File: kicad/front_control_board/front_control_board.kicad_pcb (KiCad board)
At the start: 2 copper layers, 189.2 x 48.9 mm, 67 parts, among them J1 MAIN_BOARD, J2 PROG, J3 DISPLAY, J4 LED_OUT, Q1 AO3400A, SW1 PEC11R-4215K-S00xx, SW2 BTN1, SW3 BTN4, SW4 BTN2, SW5 BTN3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

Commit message: cleanup
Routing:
- net /TXD0: track 79.4 -> 78.5 mm
- net /DOUT: track 54.2 -> 54.7 mm
- net GND: vias 47 -> 49
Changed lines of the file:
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@@
 	(title_block
 		(title "SW32 - Front Control Board")
-		(date "2024-06-02")
+		(date "2024-06-05")
 		(rev "1")
 		(company "saawsm")
@@
 	)
 	(via
-		(at 163.449 108.331)
+		(at 162.687 107.5436)
 		(size 0.6)
 		(drill 0.3)
@@
 	)
 	(via
+		(at 160.7566 109.0676)
+		(size 0.6)
+		(drill 0.3)
+		(layers "F.Cu" "B.Cu")
+		(locked yes)
+		(free yes)
+		(net 3)
+	)
+	(via
 		(at 180.34 125.603)
 		(size 0.8)
@@
 	)
 	(via
-		(at 165.735 110.617)
+		(at 165.5064 110.4392)
 		(size 0.6)
 		(drill 0.3)
@@
 	)
 	(via
+		(at 164.1856 109.0676)
+		(size 0.6)
+		(drill 0.3)
+		(layers "F.Cu" "B.Cu")
+		(locked yes)
+		(free yes)
+		(net 3)
+	)
+	(via
 		(at 177.038 95.758)
 		(size 0.6)
@@
 	)
 	(via
-		(at 162.179 110.617)
+		(at 162.0266 110.4392)
 		(size 0.6)
 		(drill 0.3)
@@
 	)
 	(via
-		(at 160.02 108.331)
+		(at 159.258 107.5436)
 		(size 0.6)
 		(drill 0.3)
@@
 	)
 	(segment
-		(start 140.335 90.7725)
-		(end 142.9925 88.115)
+		(start 139.8524 98.044)
+		(end 139.8524 91.2551)
 		(width 0.2)
 		(locked yes)
@@
 	(segment
 		(start 177.439718 112.245282)
-		(end 154.282282 112.245282)
+		(end 154.053682 112.245282)
 		(width 0.2)
 		(locked yes)
@@
 	)
 	(segment
-		(start 140.335 98.298)
-		(end 140.335 90.7725)
+		(start 139.8524 91.2551)
+		(end 142.9925 88.115)
 		(width 0.2)
 		(locked yes)
@@
 	)
 	(segment
-		(start 154.282282 112.245282)
-		(end 140.335 98.298)
+		(start 154.053682 112.245282)
+		(end 139.8524 98.044)
 		(width 0.2)
 		(locked yes)
@@
 	)
 	(segment
-		(start 154.613654 111.445282)
-		(end 141.135 97.966628)
+		(start 177.445 109.7)
+		(end 176.560599 109.7)
 		(width 0.2)
 		(locked yes)
@@
 	)
 	(segment
-		(start 177.445 109.7)
-		(end 176.560599 109.7)
+		(start 175.160999 111.0996)
+		(end 154.5336 111.0996)
 		(width 0.2)
 		(locked yes)
@@
 	)
 	(segment
-		(start 174.815317 111.445282)
-		(end 154.613654 111.445282)
+		(start 141.0208 97.5868)
+		(end 141.0208 95.1667)
 		(width 0.2)
 		(locked yes)
@@
 	)
 	(segment
-		(start 141.135 95.0525)
-		(end 142.9925 93.195)
+		(start 154.5336 111.0996)
+		(end 141.0208 97.5868)
 		(width 0.2)
 		(locked yes)
@@
 	(segment
 		(start 176.560599 109.7)
-		(end 174.815317 111.445282)
+		(end 175.160999 111.0996)
 		(width 0.2)
 		(locked yes)
@@
 	)
 	(segment
-		(start 141.135 97.966628)
-		(end 141.135 95.0525)
+		(start 141.0208 95.1667)
+		(end 142.9925 93.195)
 		(width 0.2)
 		(locked yes)
@@
 	)
 	(segment
-		(start 169.926 109.093)
-		(end 155.124686 109.093)
+		(start 168.6052 108.4326)
+		(end 155.3718 108.4326)
 		(width 0.2)
 		(locked yes)
@@
 	)
 	(segment
-		(start 145.5325 99.500814)
-		(end 145.5325 95.735)
+		(start 194.973 104.648)
+		(end 194.945 104.62)
 		(width 0.2)
 		(locked yes)
@@
 	)
 	(segment
-		(start 194.973 104.648)
-		(end 194.945 104.62)
+		(start 145.5325 98.5933)
+		(end 145.5325 95.735)
 		(width 0.2)
 		(locked yes)
@@
 	)
 	(segment
-		(start 155.124686 109.093)
-		(end 145.5325 99.500814)
+		(start 186.817 111.125)
+		(end 193.322 104.62)
 		(width 0.2)
 		(locked yes)
@@
 	)
 	(segment
-		(start 186.817 111.125)
-		(end 193.322 104.62)
+		(start 193.322 104.62)
+		(end 194.945 104.62)
 		(width 0.2)
 		(locked yes)
@@
 	)
 	(segment
-		(start 193.322 104.62)
-		(end 194.945 104.62)
+		(start 155.3718 108.4326)
+		(end 145.5325 98.5933)
 		(width 0.2)
 		(locked yes)
@@
 	)
 	(via
-		(at 169.926 109.093)
+		(at 168.6052 108.4326)
 		(size 0.6)
 		(drill 0.3)
@@
 	)
 	(segment
-		(start 169.926 109.093)
-		(end 169.926 109.728)
+		(start 168.6306 108.4326)
+		(end 173.647088 113.449088)
 		(width 0.2)
 		(locked yes)
@@
 	)
 	(segment
-		(start 169.926 109.728)
-		(end 173.647088 113.449088)
-		(width 0.2)
-		(locked yes)
-		(layer "B.Cu")
-		(net 25)
-	)
-	(segment
 		(start 180.555912 113.449088)
 		(end 180.594 113.411)
@@
 	)
 	(segment
-		(start 175.666769 111.845282)
-		(end 176.542051 110.97)
+		(start 140.4366 97.833914)
+		(end 154.286486 111.6838)
 		(width 0.2)
 		(locked yes)
@@
 	)
 	(segment
-		(start 140.735 92.9125)
-		(end 140.735 98.132314)
+		(start 140.4366 93.2109)
+		(end 140.4366 97.833914)
 		(width 0.2)
 		(locked yes)
@@
 	)
 	(segment
-		(start 176.542051 110.97)
-		(end 177.445 110.97)
+		(start 175.828251 111.6838)
+		(end 176.542051 110.97)
 		(width 0.2)
 		(locked yes)
@@
 	)
 	(segment
-		(start 142.9925 90.655)
-		(end 140.735 92.9125)
+		(start 154.286486 111.6838)
+		(end 175.828251 111.6838)
 		(width 0.2)
 		(locked yes)
@@
 	)
 	(segment
-		(start 140.735 98.132314)
-		(end 154.447968 111.845282)
+		(start 176.542051 110.97)
+		(end 177.445 110.97)
 		(width 0.2)
 		(locked yes)
@@
 	)
 	(segment
-		(start 154.447968 111.845282)
-		(end 175.666769 111.845282)
+		(start 142.9925 90.655)
+		(end 140.4366 93.2109)
 		(width 0.2)
 		(locked yes)

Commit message: move ground to center pin
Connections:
- J1 pad 1: +5V -> +3.3V
- J1 pad 2: /DOUT -> +5V
- J1 pad 3: +3.3V -> /DOUT
- J1 pad 4: /BCLK -> GND
- J1 pad 5: /RXD0 -> /BCLK
- J1 pad 8: GND -> /RXD0
- U1 pad 10: /DOUT -> /WS
- U1 pad 8: /WS -> /DOUT
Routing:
- net /DOUT: track 54.7 -> 45.0 mm
- net /BCLK: track 51.3 -> 43.0 mm
- net +3.3V: track 241.9 -> 238.8 mm
- net +5V: track 207.3 -> 209.9 mm
- net /WS: track 47.8 -> 45.7 mm
- net /TXD0: track 78.5 -> 80.4 mm
- net /RXD0: track 79.8 -> 78.9 mm
- net /CH2: track 47.9 -> 47.3 mm
- net /CH4: track 86.9 -> 87.4 mm
- net GND: vias 49 -> 55

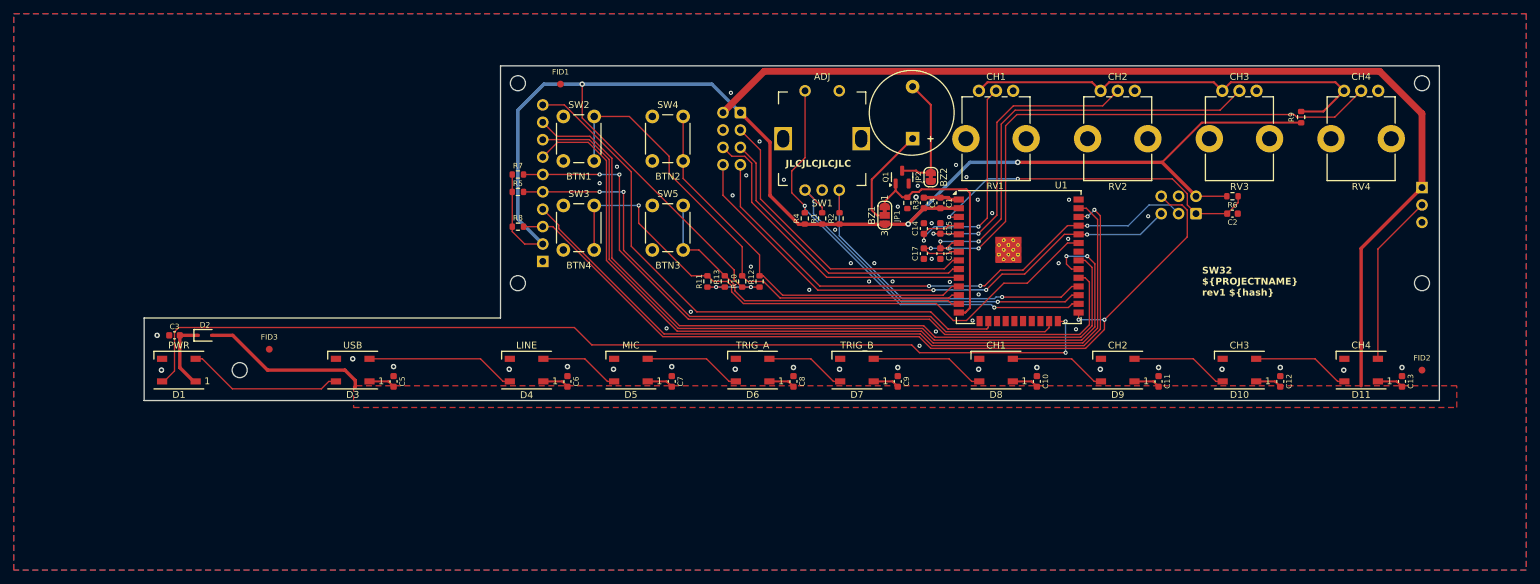
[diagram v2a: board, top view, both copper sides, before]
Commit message: unify via sizes
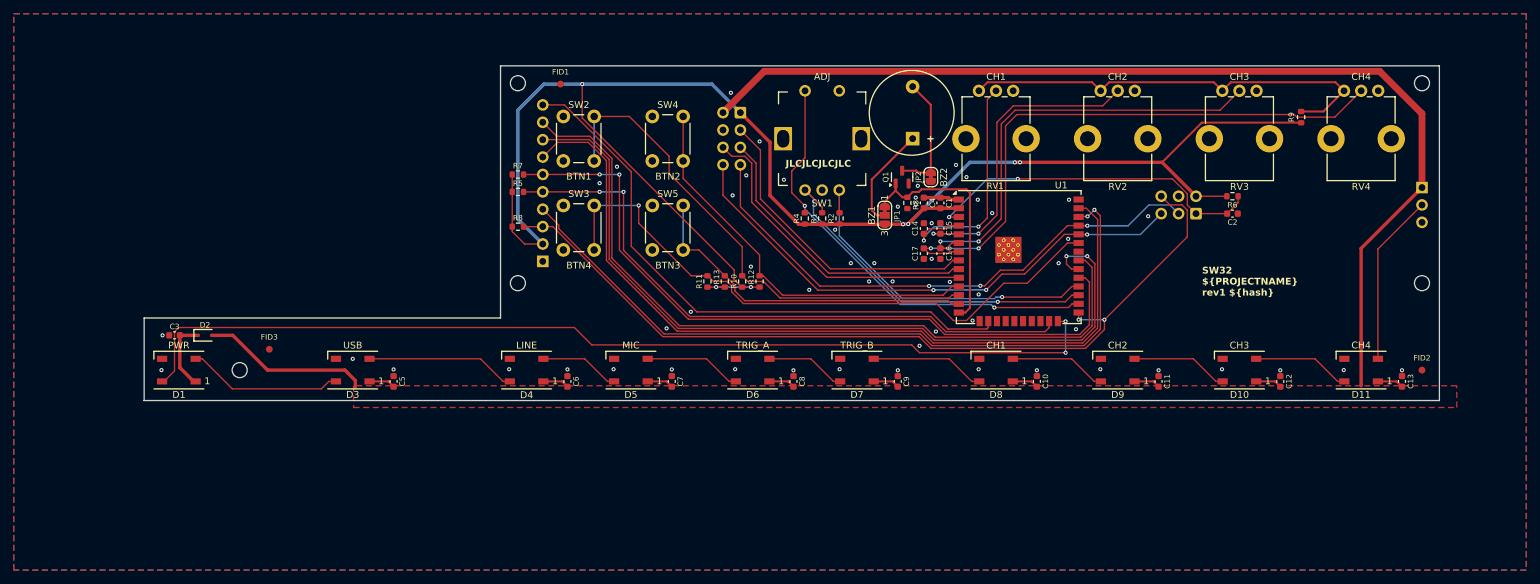
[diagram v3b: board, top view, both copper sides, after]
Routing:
- net +3.3V: track 238.8 -> 240.3 mm, vias 5 -> 7
- net GND: vias 55 -> 56
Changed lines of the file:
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@@
 	(title_block
 		(title "SW32 - Front Control Board")
-		(date "2024-06-07")
+		(date "2024-06-10")
 		(rev "1")
 		(company "saawsm")
@@
 	)
 	(via
-		(at 60.325 120.65)
-		(size 0.8)
-		(drill 0.4)
+		(at 61.1124 120.65)
+		(size 0.6)
+		(drill 0.3)
 		(layers "F.Cu" "B.Cu")
 		(locked yes)
@@
 	)
 	(via
-		(at 120.269 125.222)
-		(size 0.8)
-		(drill 0.4)
+		(at 120.269 125.6284)
+		(size 0.6)
+		(drill 0.3)
 		(layers "F.Cu" "B.Cu")
 		(locked yes)
@@
 	(via
 		(at 60.96 125.73)
-		(size 0.8)
-		(drill 0.4)
+		(size 0.6)
+		(drill 0.3)
 		(layers "F.Cu" "B.Cu")
 		(locked yes)
@@
 	)
 	(via
-		(at 188.849 125.349)
-		(size 0.8)
-		(drill 0.4)
+		(at 188.849 125.7554)
+		(size 0.6)
+		(drill 0.3)
 		(layers "F.Cu" "B.Cu")
 		(locked yes)
@@
 	)
 	(via
-		(at 206.629 125.349)
-		(size 0.8)
-		(drill 0.4)
+		(at 206.629 125.7554)
+		(size 0.6)
+		(drill 0.3)
 		(layers "F.Cu" "B.Cu")
 		(locked yes)
@@
 	(via
 		(at 144.78 125.603)
-		(size 0.8)
-		(drill 0.4)
+		(size 0.6)
+		(drill 0.3)
 		(layers "F.Cu" "B.Cu")
 		(locked yes)
@@
 	)
 	(via
-		(at 135.509 125.222)
-		(size 0.8)
-		(drill 0.4)
+		(at 135.509 125.6284)
+		(size 0.6)
+		(drill 0.3)
 		(layers "F.Cu" "B.Cu")
 		(locked yes)
@@
 	(via
 		(at 215.9 125.603)
-		(size 0.8)
-		(drill 0.4)
+		(size 0.6)
+		(drill 0.3)
 		(layers "F.Cu" "B.Cu")
 		(locked yes)
@@
 	(via
 		(at 180.34 125.603)
-		(size 0.8)
-		(drill 0.4)
+		(size 0.6)
+		(drill 0.3)
 		(layers "F.Cu" "B.Cu")
 		(locked yes)
@@
 	)
 	(via
-		(at 168.529 125.349)
-		(size 0.8)
-		(drill 0.4)
+		(at 168.529 125.7554)
+		(size 0.6)
+		(drill 0.3)
 		(layers "F.Cu" "B.Cu")
 		(locked yes)
@@
 	(via
 		(at 111.76 125.603)
-		(size 0.8)
-		(drill 0.4)
+		(size 0.6)
+		(drill 0.3)
 		(layers "F.Cu" "B.Cu")
 		(locked yes)
@@
 	(via
 		(at 88.9 124.079)
-		(size 0.8)
-		(drill 0.4)
+		(size 0.6)
+		(drill 0.3)
 		(layers "F.Cu" "B.Cu")
 		(locked yes)
@@
 	)
 	(via
-		(at 171.196 100.46012)
-		(size 0.8)
-		(drill 0.4)
+		(at 171.1452 100.5332)
+		(size 0.6)
+		(drill 0.3)
 		(layers "F.Cu" "B.Cu")
 		(locked yes)
@@
 	)
 	(via
-		(at 224.409 125.349)
-		(size 0.8)
-		(drill 0.4)
+		(at 224.409 125.7554)
+		(size 0.6)
+		(drill 0.3)
 		(layers "F.Cu" "B.Cu")
 		(locked yes)
@@
 	)
 	(via
-		(at 242.189 125.349)
-		(size 0.8)
-		(drill 0.4)
+		(at 242.189 125.7554)
+		(size 0.6)
+		(drill 0.3)
 		(layers "F.Cu" "B.Cu")
 		(locked yes)
@@
 	)
 	(via
-		(at 94.869 125.222)
-		(size 0.8)
-		(drill 0.4)
+		(at 94.869 125.6284)
+		(size 0.6)
+		(drill 0.3)
 		(layers "F.Cu" "B.Cu")
 		(locked yes)
@@
 	(via
 		(at 127 125.603)
-		(size 0.8)
-		(drill 0.4)
+		(size 0.6)
+		(drill 0.3)
 		(layers "F.Cu" "B.Cu")
 		(locked yes)
@@
 	(via
 		(at 160.02 125.603)
-		(size 0.8)
-		(drill 0.4)
+		(size 0.6)
+		(drill 0.3)
+		(layers "F.Cu" "B.Cu")
+		(locked yes)
+		(free yes)
+		(net 3)
+	)
+	(via
+		(at 171.1452 101.4984)
+		(size 0.6)
+		(drill 0.3)
 		(layers "F.Cu" "B.Cu")
 		(locked yes)
@@
 	)
 	(via
-		(at 153.289 125.349)
-		(size 0.8)
-		(drill 0.4)
+		(at 153.289 125.7554)
+		(size 0.6)
+		(drill 0.3)
 		(layers "F.Cu" "B.Cu")
 		(locked yes)
@@
 	(via
 		(at 233.68 125.73)
-		(size 0.8)
-		(drill 0.4)
+		(size 0.6)
+		(drill 0.3)
 		(layers "F.Cu" "B.Cu")
 		(locked yes)
@@
 	(via
 		(at 198.12 125.603)
-		(size 0.8)
-		(drill 0.4)
+		(size 0.6)
+		(drill 0.3)
 		(layers "F.Cu" "B.Cu")
 		(locked yes)
@@
 	)
 	(segment
+		(start 185.6232 95.377)
+		(end 186.3852 95.377)
+		(width 0.5)
+		(locked yes)
+		(layer "F.Cu")
+		(net 4)
+	)
+	(segment
 		(start 147.002 113.601)
 		(end 145.796 113.601)
@@
 	)
 	(segment
+		(start 186.3852 95.377)
+		(end 207.142 95.377)
+		(width 0.5)
+		(locked yes)
+		(layer "F.Cu")
+		(net 4)
+	)
+	(segment
 		(start 122.428 83.947)
 		(end 122.428 88.9)
@@
 		(net 4)
 	)
-	(segment
-		(start 186.055 95.377)
-		(end 207.142 95.377)
-		(width 0.5)
+	(via
+		(at 186.3852 95.377)
+		(size 0.6)
+		(drill 0.3)
+		(layers "F.Cu" "B.Cu")
+		(locked yes)
+		(net 4)
+	)
+	(via
+		(at 169.299892 104.426093)
+		(size 0.6)
+		(drill 0.3)
+		(layers "F.Cu" "B.Cu")
 		(locked yes)
-		(layer "F.Cu")
 		(net 4)
 	)
 	(via
-		(at 186.055 95.377)
-		(size 0.8)
-		(drill 0.4)
+		(at 185.6232 95.377)
+		(size 0.6)
+		(drill 0.3)
 		(layers "F.Cu" "B.Cu")
 		(locked yes)
@@
 	(via
 		(at 122.428 83.947)
-		(size 0.8)
-		(drill 0.4)
+		(size 0.6)
+		(drill 0.3)
 		(layers "F.Cu" "B.Cu")
 		(locked yes)
@@
 	(via
 		(at 170.053 104.394)
-		(size 0.8)
-		(drill 0.4)
+		(size 0.6)
+		(drill 0.3)
 		(layers "F.Cu" "B.Cu")
 		(locked yes)
@@
 	)
 	(segment
+		(start 186.3852 95.377)
+		(end 179.07 95.377)
+		(width 0.5)
+		(locked yes)
+		(layer "B.Cu")
+		(net 4)
+	)
+	(segment
+		(start 169.299892 104.426093)
+		(end 170.020907 104.426093)
+		(width 0.5)
+		(locked yes)
+		(layer "B.Cu")
+		(net 4)
+	)
+	(segment
+		(start 170.020907 104.426093)
+		(end 170.053 104.394)
+		(width 0.5)
+		(locked yes)
+		(layer "B.Cu")
+		(net 4)
+	)
+	(segment
 		(start 122.428 83.947)
 		(end 141.3645 83.947)
@@
 		(width 0.5)
 		(locked yes)
-		(layer "B.Cu")
-		(net 4)
-	)
-	(segment
-		(start 186.055 95.377)
-		(end 179.07 95.377)
-		(width 0.5)
-		(locked yes)

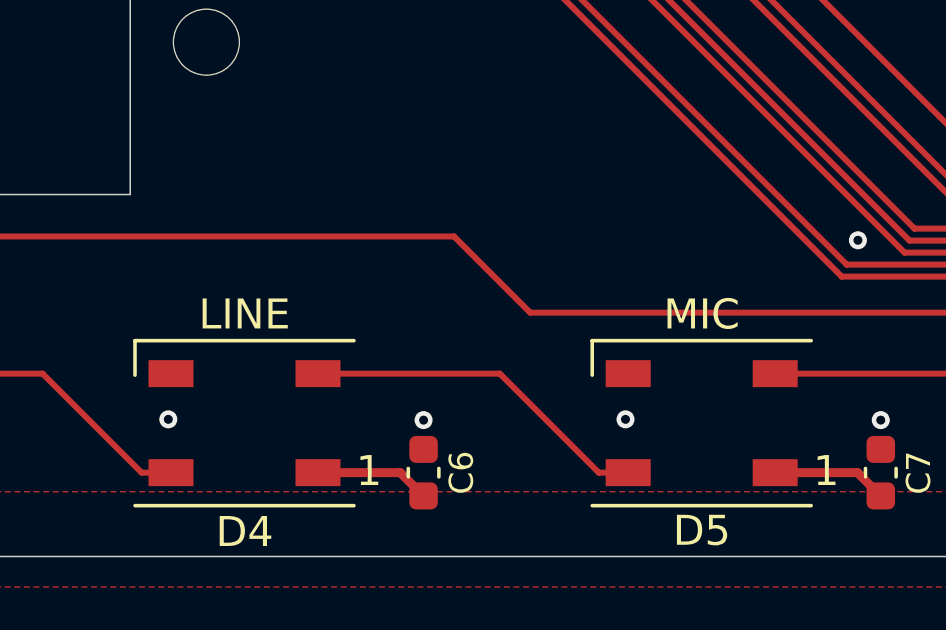
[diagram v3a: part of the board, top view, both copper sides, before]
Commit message: fix LED order
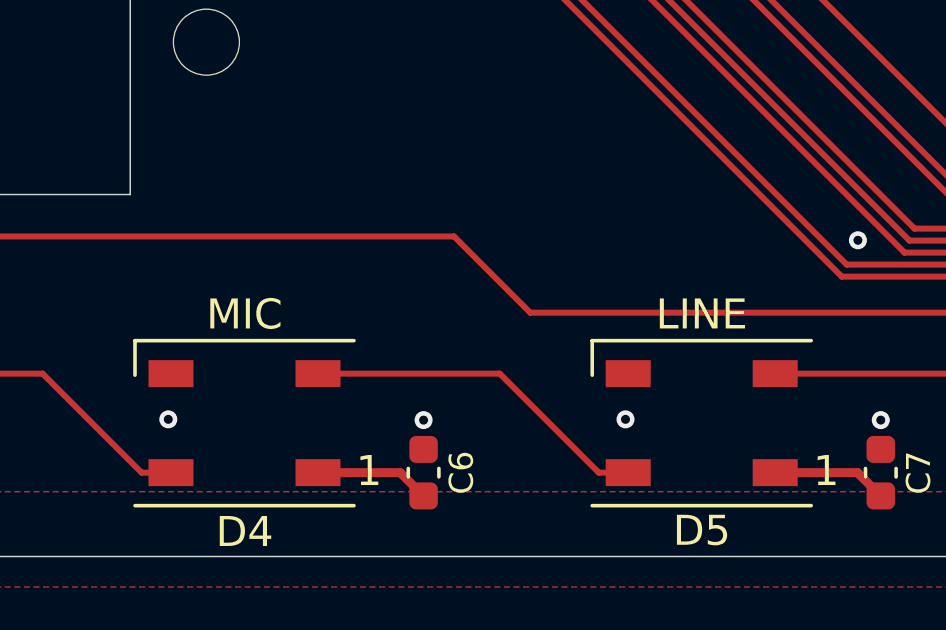
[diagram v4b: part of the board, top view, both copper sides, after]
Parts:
- D4: value LINE -> MIC
- D5: value MIC -> LINE
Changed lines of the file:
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@@
 	(title_block
 		(title "SW32 - Front Control Board")
-		(date "2024-06-10")
+		(date "2024-06-11")
 		(rev "1")
 		(company "saawsm")
@@
 			)
 		)
-		(property "Value" "LINE"
+		(property "Value" "MIC"
 			(at 0.00034 3.620248 180)
 			(layer "F.SilkS")
@@
 			)
 		)
-		(property "Value" "MIC"
+		(property "Value" "LINE"
 			(at 0.00034 3.620248 180)
 			(layer "F.SilkS")

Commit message: fix title block
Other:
- board text added: "${TITLE} ${PROJECTNAME} rev${REVISION} ${hash}"
- board text removed: "SW32 ${PROJECTNAME} rev${REVISION} ${hash}"
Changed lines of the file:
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@@
 	(paper "A4")
 	(title_block
-		(title "SW32 - Front Control Board")
-		(date "2024-06-11")
+		(title "SW32")
+		(date "2024-06-12")
 		(rev "1")
 		(company "saawsm")
@@
 		)
 	)
-	(gr_text "SW32\n${PROJECTNAME} \nrev${REVISION} ${hash}"
+	(gr_text "${TITLE}\n${PROJECTNAME} \nrev${REVISION} ${hash}"
 		(locked yes)
 		(at 212.979 112.776 0)

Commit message: add plot settings
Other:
- board text added: "${TITLE} ${PROJECTNAME} rev${REVISION}"
- board text removed: "${TITLE} ${PROJECTNAME} rev${REVISION} ${hash}"
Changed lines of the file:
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@@
 			(plot_on_all_layers_selection 0x0000000_00000000)
 			(disableapertmacros no)
-			(usegerberextensions no)
-			(usegerberattributes yes)
-			(usegerberadvancedattributes yes)
-			(creategerberjobfile yes)
+			(usegerberextensions yes)
+			(usegerberattributes no)
+			(usegerberadvancedattributes no)
+			(creategerberjobfile no)
 			(dashed_line_dash_ratio 12.000000)
 			(dashed_line_gap_ratio 3.000000)
@@
 			(plotinvisibletext no)
 			(sketchpadsonfab no)
-			(subtractmaskfromsilk no)
+			(subtractmaskfromsilk yes)
 			(outputformat 1)
 			(mirror no)
-			(drillshape 1)
+			(drillshape 0)
 			(scaleselection 1)
-			(outputdirectory "")
+			(outputdirectory "../../pcb/front_control_board/")
 		)
 	)
@@
 		)
 	)
-	(gr_text "${TITLE}\n${PROJECTNAME} \nrev${REVISION} ${hash}"
+	(gr_text "${TITLE}\n${PROJECTNAME} \nrev${REVISION}"
 		(locked yes)
 		(at 212.979 112.776 0)
